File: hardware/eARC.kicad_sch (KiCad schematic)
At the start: 1 part, among them IC3 SII9437CNUC

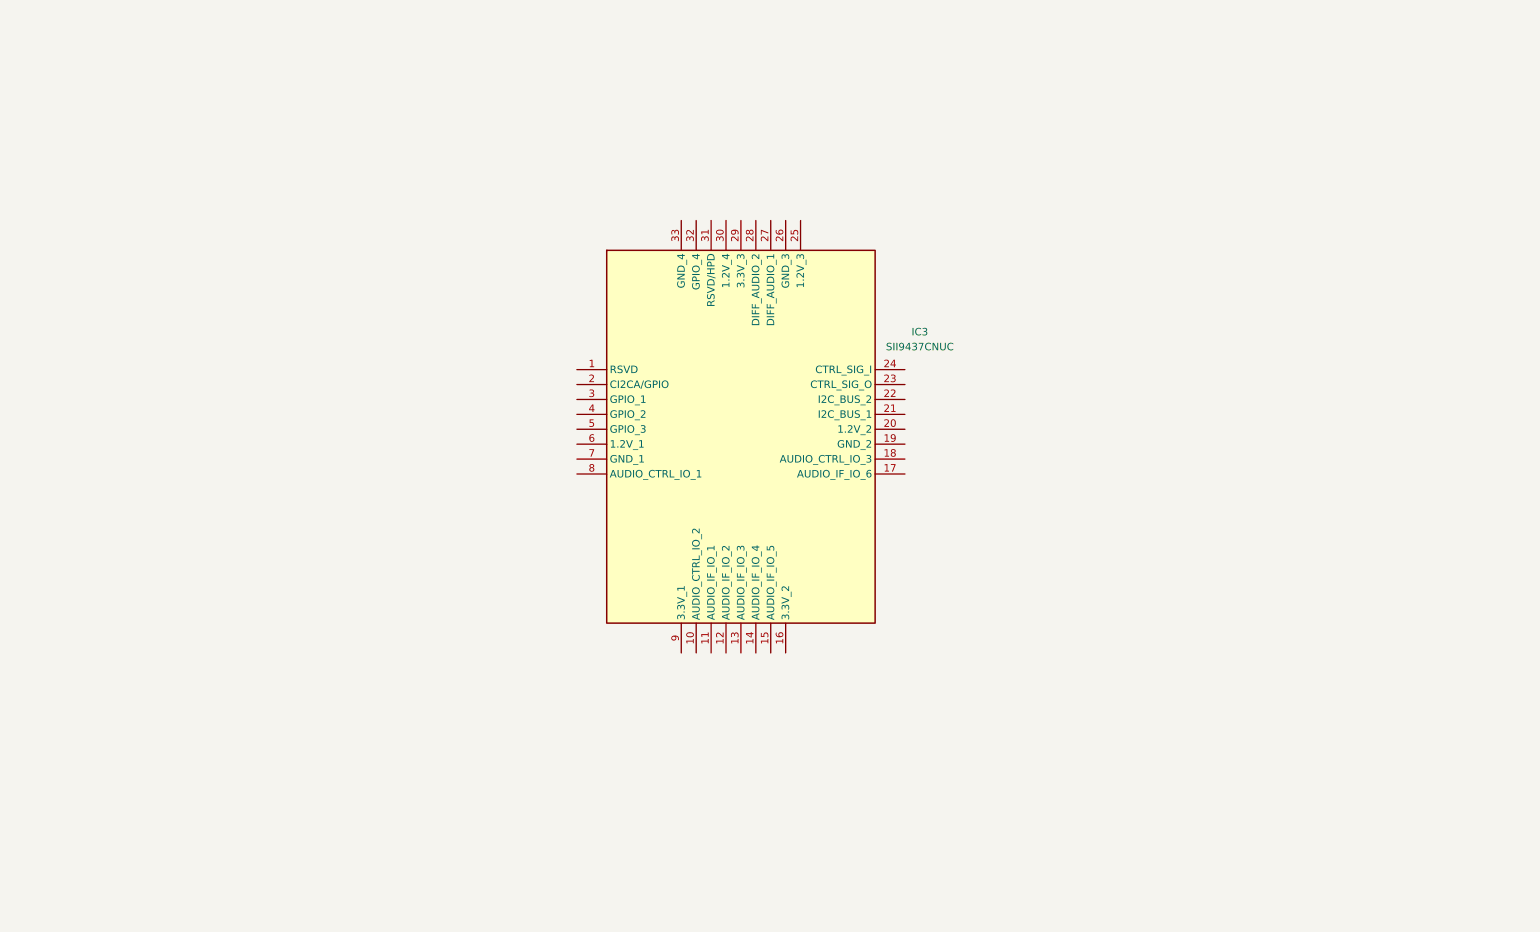
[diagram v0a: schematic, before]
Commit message: finished eARC and started with DSP
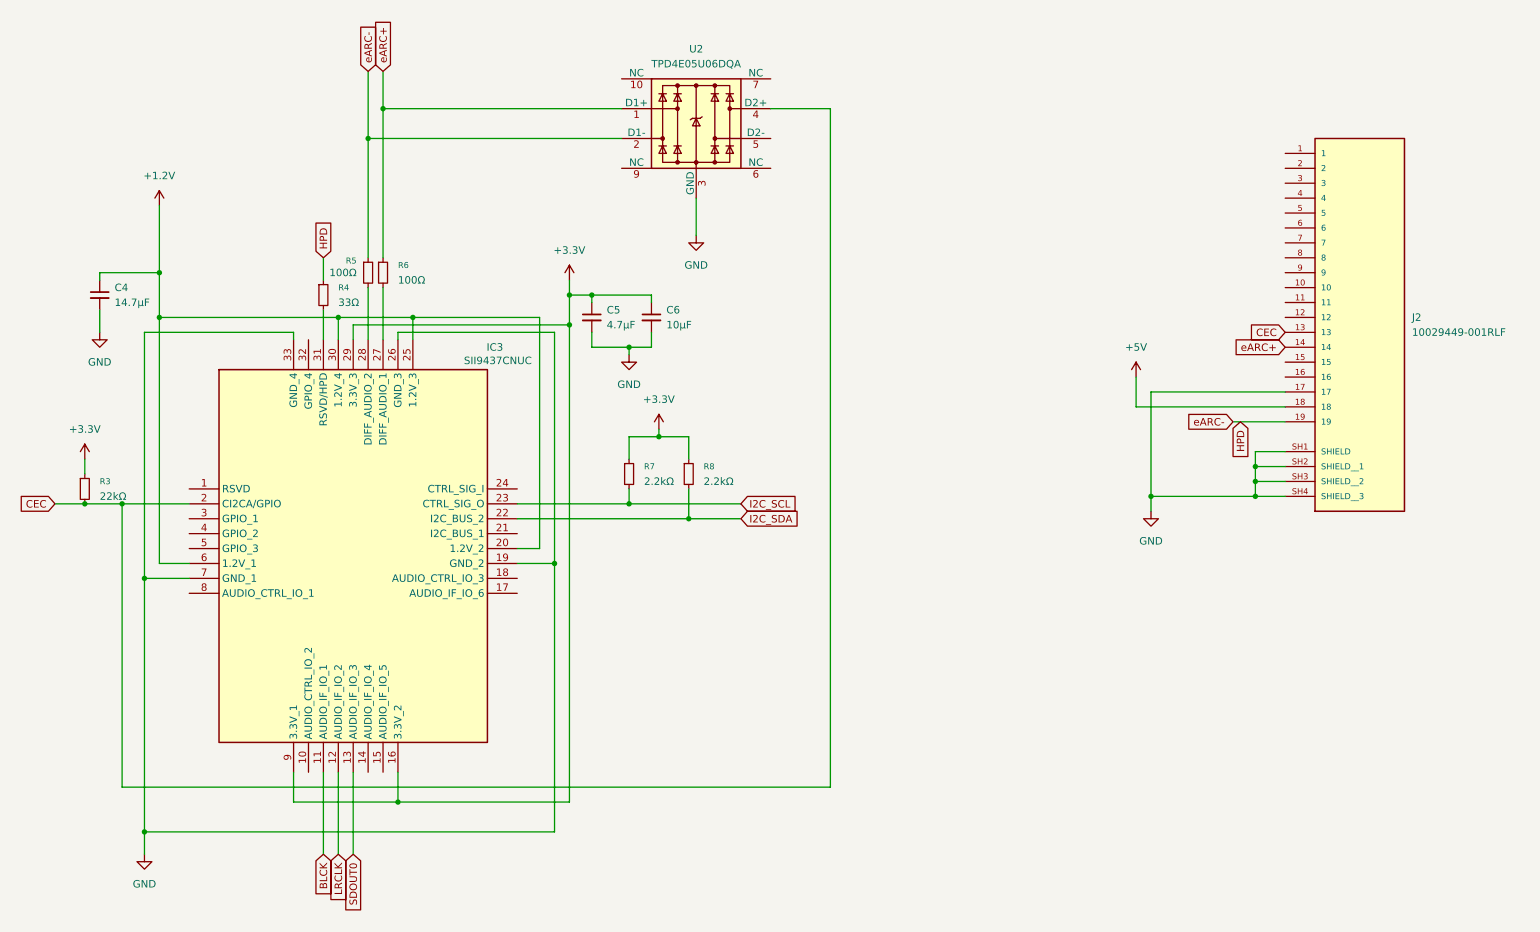
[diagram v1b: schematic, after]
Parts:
- added C4: 14.7μF, symbol Device:C_Small
- added C5: 4.7μF, symbol Device:C_Small
- added C6: 10μF, symbol Device:C_Small
- added J2: 10029449-001RLF, 10029449-001RLF:AMPHENOL_10029449-001RLF, symbol piavr:10029449-001RLF
- added R3: 22kΩ, symbol Device:R_Small
- added R4: 33Ω, symbol Device:R_Small
- added R5, R6: 100Ω, symbol Device:R_Small
- added R7, R8: 2.2kΩ, symbol Device:R_Small
- added U2: TPD4E05U06DQA, Package_SON:USON-10_2.5x1.0mm_P0.5mm, symbol Power_Protection:TPD4E05U06DQA
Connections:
- net BLCK: now reaches IC3.11 (AUDIO_IF_IO_1)
- net LRCLK: now reaches IC3.12 (AUDIO_IF_IO_2)
- net SDOUT0: now reaches IC3.13 (AUDIO_IF_IO_3)
- net +3.3V: now reaches IC3.16 (3.3V_2)
- net +3.3V: now also IC3.29 (3.3V_3), IC3.9 (3.3V_1), C5.1, C6.1, R3.1, R7.1, R8.1
- net GND: now reaches IC3.19 (GND_2)
- net GND: now also IC3.26 (GND_3), IC3.33 (GND_4), IC3.7 (GND_1), C4.2, C5.2, C6.2, J2.17, J2.SH1 (SHIELD), J2.SH2 (SHIELD__1), J2.SH3 (SHIELD__2), J2.SH4 (SHIELD__3), U2.3 (GND), U2.8 (GND)
- net CEC: now reaches IC3.2 (CI2CA/GPIO)
- net CEC: now also J2.13, R3.2, U2.4 (D2+)
- net +1.2V: now reaches IC3.20 (1.2V_2)
- net +1.2V: now also IC3.25 (1.2V_3), IC3.30 (1.2V_4), IC3.6 (1.2V_1), C4.1
- net I2C_SDA: now reaches IC3.22 (I2C_BUS_2)
- net I2C_SDA: now also R8.2
- net I2C_SCL: now reaches IC3.23 (CTRL_SIG_O)
- net I2C_SCL: now also R7.2
- net at IC3.27 (DIFF_AUDIO_1): now also R6.2
- net at IC3.28 (DIFF_AUDIO_2): now also R5.2
- net at IC3.31 (RSVD/HPD): now also R4.2
- new net +5V: J2.18
- new net HPD: J2.19, R4.1, R5.1, U2.2 (D1-)
- new net eARC+: J2.14, R6.1, U2.1 (D1+)
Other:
- moved on the sheet: IC3
